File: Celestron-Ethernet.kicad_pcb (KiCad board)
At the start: 4 copper layers, 88.9 x 31.8 mm, 61 parts, among them J1 FTDI, J2 RJ45_Amphenol_RJMG1BD3B8K1ANR, J3 6P6C, SW1 SW_Push, SW2 SW_DIP_x02, U1 W5500, U2 ATmega328P-AU, U3 74AHC1G125, U4 NCV33375ST-3.3, Y1 8MHz, Y2 25MHz

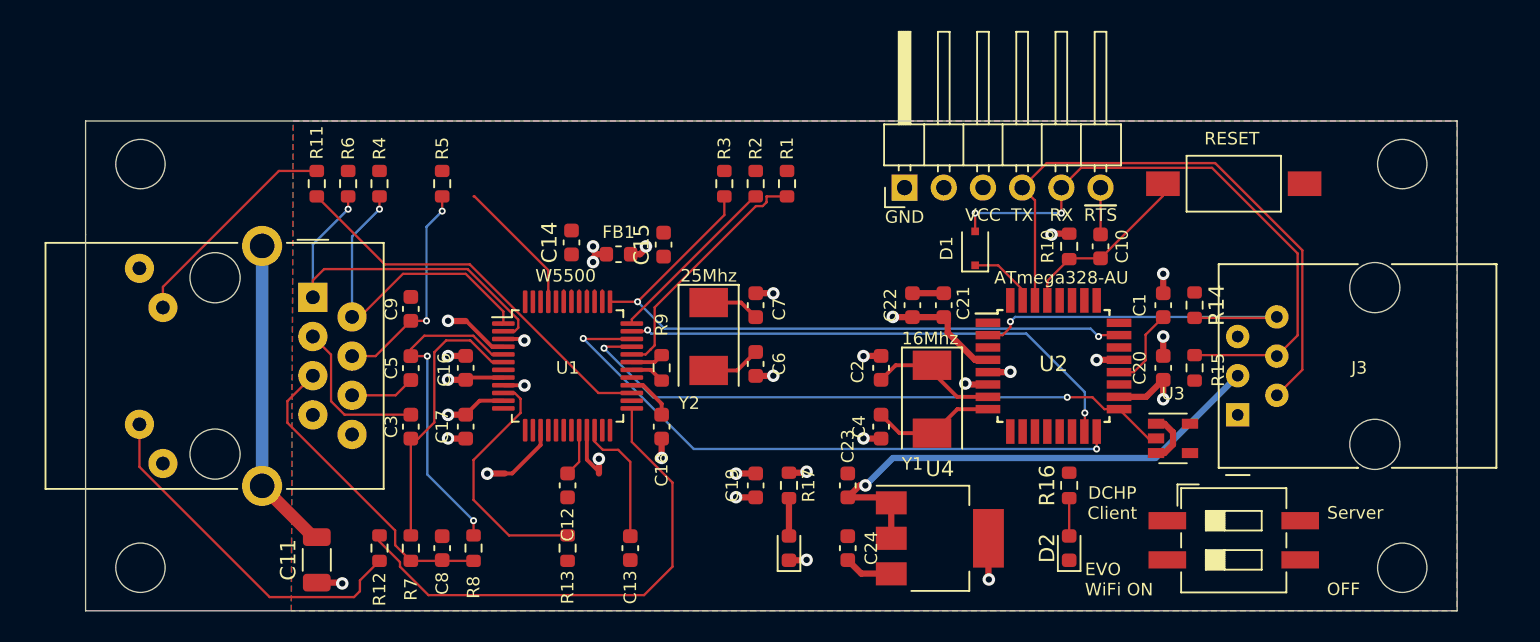
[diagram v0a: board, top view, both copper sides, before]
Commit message: Added GPS connectors
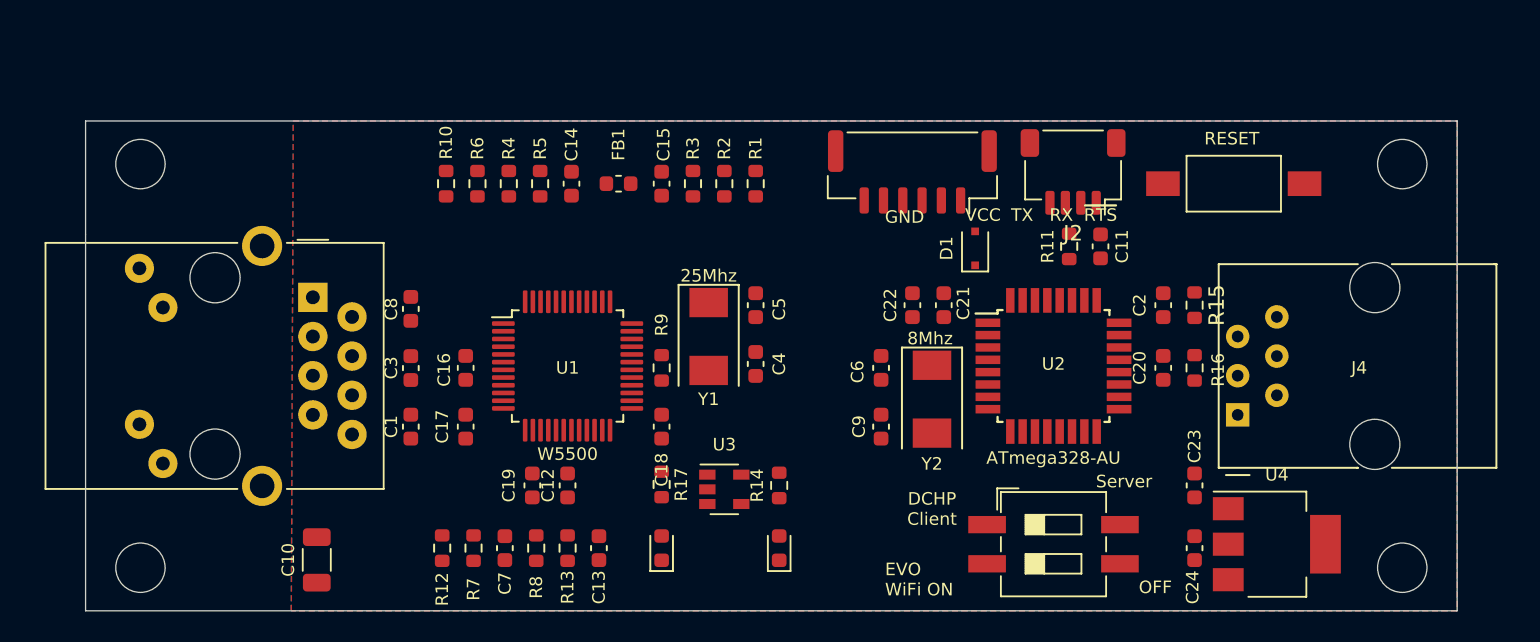
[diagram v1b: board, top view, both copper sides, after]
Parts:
- removed the C11 at (116.6, 111.0)
- removed the C6 at (145.0, 98.3)
- removed the C9 at (122.7, 94.7)
- removed the R11 at (116.6, 86.6)
- removed the R16 at (165.4, 106.2)
- removed the Y2 at (142.0, 96.5)
- added C1: 6.8nF, Capacitor_SMD:C_0603_1608Metric, F.Cu at (122.7, 102.4)
- added C10: 1nF/2KV, Capacitor_SMD:C_1206_3216Metric, F.Cu at (116.6, 111.0)
- added C4: 18pF, Capacitor_SMD:C_0603_1608Metric, F.Cu at (145.0, 98.3)
- added J3: RJ45_Amphenol_RJMG1BD3B8K1ANR, Connector_RJ:RJ45_Amphenol_RJMG1BD3B8K1ANR, F.Cu at (116.3, 94.0)
- added R10: 330R, Resistor_SMD:R_0603_1608Metric, F.Cu at (125.0, 86.6)
- added R14: 330R, Resistor_SMD:R_0603_1608Metric, F.Cu at (146.6, 106.2)
- added Y1: 25MHz, Crystal:Crystal_SMD_0603-2Pin_6.0x3.5mm, F.Cu at (142.0, 96.5)
- C5: value 6.8nF -> 18pF
- C7: value 18pF -> 10nF
- C8: value 10nF -> 22nF
- J1: footprint Connector_PinHeader_2.54mm:PinHeader_1x06_P2.54mm_Horizontal -> Connector_JST:JST_GH_SM06B-GHS-TB_1x06-1MP_P1.25mm_Horizontal
- J2: value RJ45_Amphenol_RJMG1BD3B8K1ANR -> Conn_01x04; footprint Connector_RJ:RJ45_Amphenol_RJMG1BD3B8K1ANR -> Connector_JST:JST_SH_SM04B-SRSS-TB_1x04-1MP_P1.00mm_Horizontal
- moved J2 49.9 mm to (165.6, 85.9), turned to 180 degrees
- moved U3 29.3 mm to (143.0, 106.4)
- moved C5 22.7 mm to (145.0, 94.5), turned to 270 degrees
- moved C7 22.6 mm to (128.8, 110.2)
- moved C23 22.5 mm to (173.5, 106.2)
- moved C24 22.5 mm to (173.5, 110.2)
- moved U4 21.8 mm to (178.8, 110.0)
- moved D2 18.8 mm to (146.6, 110.2)
- moved C8 15.6 mm to (122.7, 94.7)
- moved C19 14.5 mm to (130.6, 106.2)
- moved SW1 11.7 mm to (164.3, 110.0)
- moved R4 8.38 mm to (129.0, 86.6)
- moved R6 8.38 mm to (127.0, 86.6)
- moved R17 8.26 mm to (138.9, 106.1)
- moved D3 8.26 mm to (138.9, 110.2)
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- renumbered C10 to C11, C1 to C2, C2 to C6, C4 to C9, J3 to J4, R10 to R11, R14 to R15, R15 to R16, SW2 to SW1, SW1 to SW2, Y1 to Y2
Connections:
- net /D8 renamed /BUSY
- C3 pad 1: /RX+ -> /RD-
- C3 pad 2: /RD+ -> /RX-
- C5 pad 1: /RD- -> GND
- C5 pad 2: /RX- -> Net-(C5-Pad2)
- C7 pad 2: Net-(C7-Pad2) -> /RCT
- C8 pad 2: /RCT -> /TCT
- J1 pad 1: GND -> (no net)
- J1 pad 3: VCC -> /GTX
- J1 pad 4: /RXI -> /GRX
- J1 pad 5: /TXO -> VCC
- J1 pad 6: /DTR -> (no net)
- J4 pad 1: Net-(J3-Pad1) -> /DTR
- R9 pad 1: Net-(C7-Pad2) -> Net-(C5-Pad2)
- U1 pad 12: Net-(U1-Pad12) -> (no net)
- U1 pad 13: Net-(U1-Pad13) -> (no net)
- U1 pad 18: Net-(U1-Pad18) -> (no net)
- U1 pad 24: Net-(U1-Pad24) -> (no net)
- U1 pad 26: Net-(U1-Pad26) -> (no net)
- U1 pad 31: Net-(C7-Pad2) -> Net-(C5-Pad2)
- U1 pad 46: Net-(U1-Pad46) -> (no net)
- U1 pad 47: Net-(U1-Pad47) -> (no net)
- U1 pad 7: Net-(U1-Pad7) -> (no net)
- U2 pad 1: Net-(U2-Pad1) -> (no net)
- U2 pad 10: Net-(U2-Pad10) -> /GRX
- U2 pad 11: Net-(U2-Pad11) -> /GTX
- U2 pad 13: Net-(U2-Pad13) -> (no net)
- U2 pad 14: Net-(U2-Pad14) -> (no net)
- U2 pad 19: Net-(U2-Pad19) -> (no net)
- U2 pad 22: Net-(U2-Pad22) -> (no net)
- U2 pad 24: Net-(U2-Pad24) -> (no net)
- U2 pad 25: Net-(U2-Pad25) -> (no net)
- U2 pad 26: Net-(U2-Pad26) -> (no net)
- U2 pad 27: Net-(U2-Pad27) -> (no net)
- U2 pad 28: Net-(U2-Pad28) -> (no net)
- U2 pad 32: Net-(U2-Pad32) -> (no net)
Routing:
- net /~RST: track 43.1 -> 0.00 mm, vias 2 -> 0
- net /MISO: track 40.5 -> 0.00 mm, vias 2 -> 0
- net /SCK: track 40.0 -> 0.00 mm, vias 2 -> 0
- net /TXO: track 39.2 -> 0.00 mm, vias 2 -> 0
- net /RXI: track 38.9 -> 0.00 mm
- net VCC: track 34.8 -> 0.00 mm, vias 7 -> 0
- net +12V: track 34.1 -> 0.00 mm, vias 1 -> 0
- net /MOSI: track 33.6 -> 0.00 mm, vias 2 -> 0
- net /LINKLED: track 33.1 -> 0.00 mm
- net GND: track 32.3 -> 0.00 mm, vias 17 -> 0
- net /ACTLED: track 25.7 -> 0.00 mm
- net /TD+: track 25.2 -> 0.00 mm, vias 1 -> 0
- net /BUSY: track 24.8 -> 0.00 mm, vias 1 -> 0
- net /LEDY_K: track 23.2 -> 0.00 mm
- net +3.3VA: track 23.0 -> 0.00 mm, vias 7 -> 0
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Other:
- board text added: "8Mhz"
- board text removed: "16Mhz"

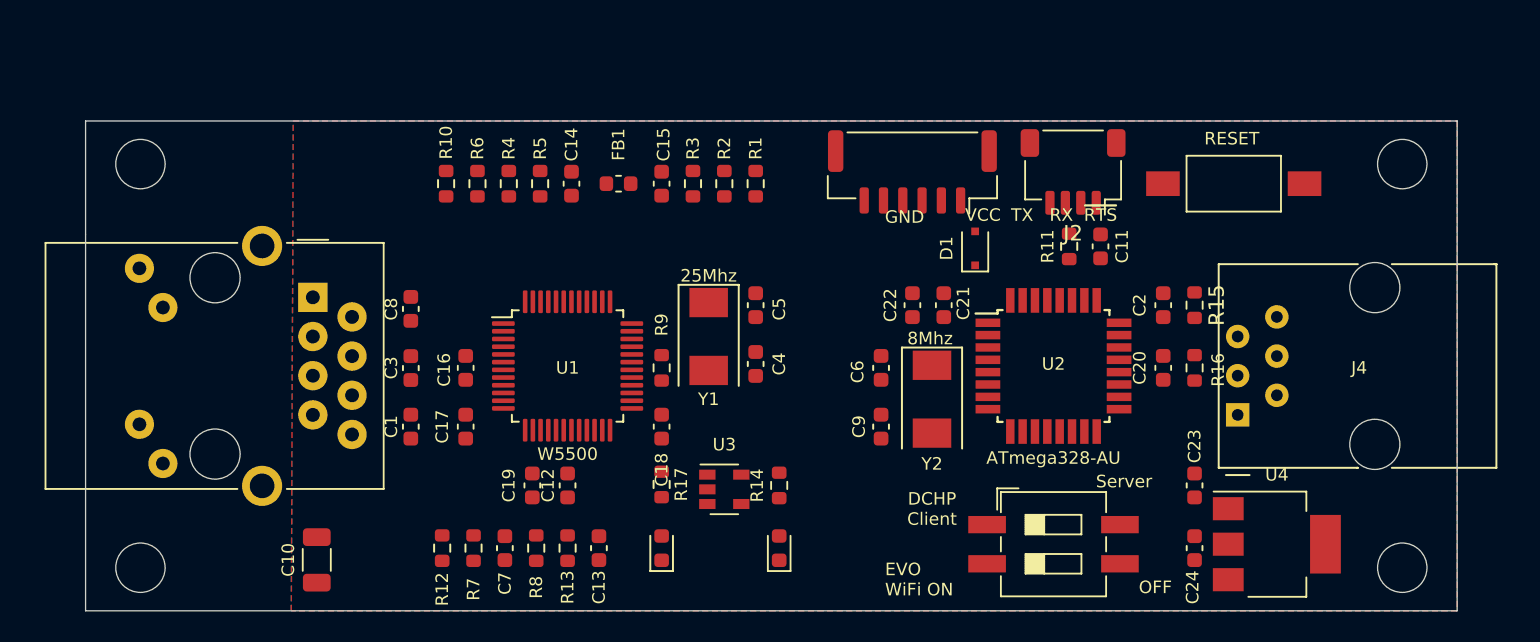
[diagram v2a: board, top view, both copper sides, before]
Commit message: W5500 fixes
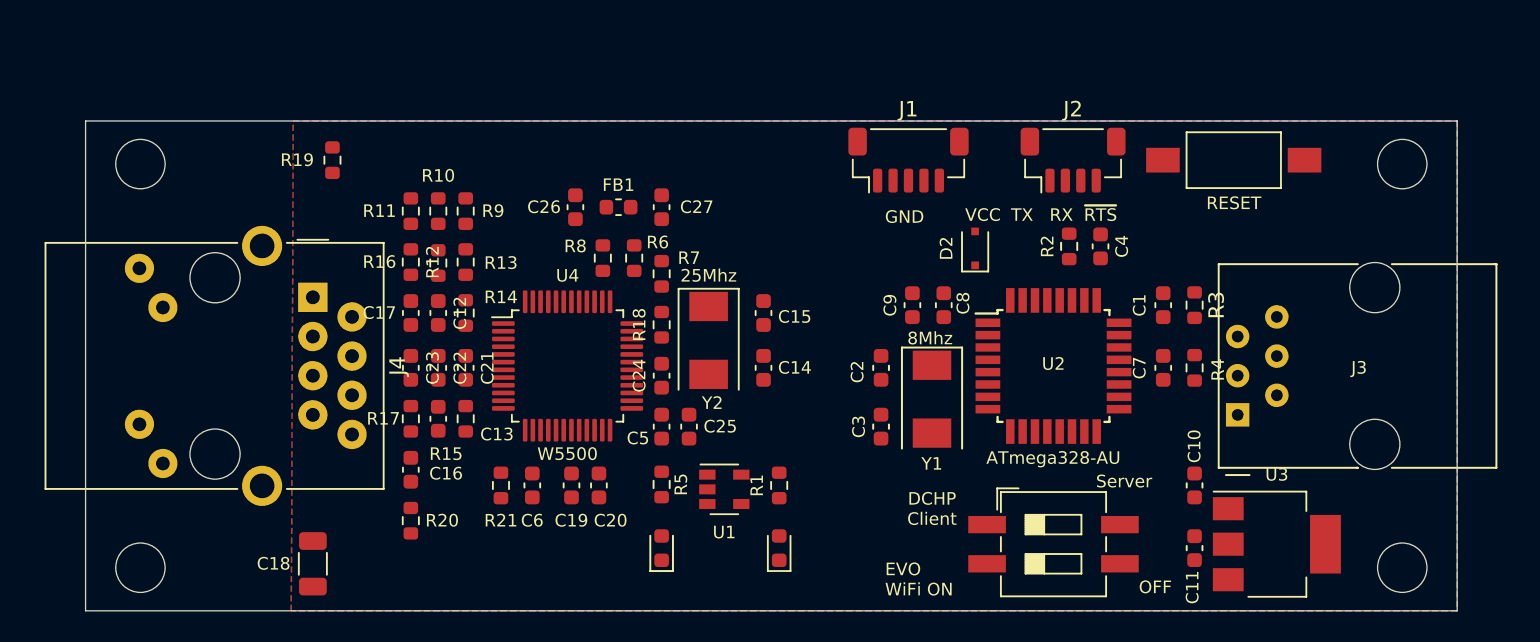
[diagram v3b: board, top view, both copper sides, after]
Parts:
- removed the C1 at (122.7, 102.4)
- removed the C10 at (116.6, 111.0)
- removed the C3 at (122.7, 98.6)
- removed the C4 at (145.0, 98.3)
- removed the C5 at (145.0, 94.5)
- removed the C7 at (128.8, 110.2)
- removed the C8 at (122.7, 94.7)
- removed the J3 at (116.3, 94.0)
- removed the R1 at (145.0, 86.6)
- removed the R2 at (143.0, 86.6)
- removed the R3 at (141.0, 86.6)
- removed the R4 at (129.0, 86.6)
- removed the R5 at (131.1, 86.6)
- removed the U1 at (132.8, 98.4)
- removed the Y1 at (142.0, 96.5)
- added C18: 1nF/2KV, Capacitor_SMD:C_1206_3216Metric, F.Cu at (116.3, 111.3)
- added C19: 4.7uF, Capacitor_SMD:C_0603_1608Metric, F.Cu at (133.1, 106.2)
- added C20: 10nF, Capacitor_SMD:C_0603_1608Metric, F.Cu at (134.9, 106.2)
- added C21: 100nF, Capacitor_SMD:C_0603_1608Metric, F.Cu at (126.2, 98.6)
- added C22: 1uF, Capacitor_SMD:C_0603_1608Metric, F.Cu at (124.5, 98.6)
- added C23: 10uF, Capacitor_SMD:C_0603_1608Metric, F.Cu at (122.7, 98.6)
- added C24: 100nF, Capacitor_SMD:C_0603_1608Metric, F.Cu at (138.9, 99.1)
- added C25: 10uF, Capacitor_SMD:C_0603_1608Metric, F.Cu at (140.7, 102.4)
- added C26: 100nF, Capacitor_SMD:C_0603_1608Metric, F.Cu at (133.3, 88.1)
- added C27: 100nF, Capacitor_SMD:C_0603_1608Metric, F.Cu at (138.9, 88.1)
- added J4: RJ45_Amphenol_RJMG1BD3B8K1ANR, Connector_RJ:RJ45_Amphenol_RJMG1BD3B8K1ANR, F.Cu at (116.3, 94.0)
- added R11: 49R9, Resistor_SMD:R_0603_1608Metric, F.Cu at (122.7, 88.4)
- added R14: 3R3, Resistor_SMD:R_0603_1608Metric, F.Cu at (126.2, 95.0)
- added R15: 3R3, Resistor_SMD:R_0603_1608Metric, F.Cu at (126.2, 101.9)
- added R16: 49R9, Resistor_SMD:R_0603_1608Metric, F.Cu at (126.2, 91.7)
- added R17: 49R9, Resistor_SMD:R_0603_1608Metric, F.Cu at (122.7, 101.9)
- added R18: 1M, Resistor_SMD:R_0603_1608Metric, F.Cu at (138.9, 95.8)
- added R19: 330R, Resistor_SMD:R_0603_1608Metric, F.Cu at (117.6, 85.1)
- added R20: 330R, Resistor_SMD:R_0603_1608Metric, F.Cu at (122.7, 108.5)
- added R21: 12.4K, Resistor_SMD:R_0603_1608Metric, F.Cu at (128.5, 106.2)
- added U4: W5500, Package_QFP:LQFP-48_7x7mm_P0.5mm, F.Cu at (132.8, 98.4)
- added Y2: 25MHz, Crystal:Crystal_SMD_0603-2Pin_6.0x3.5mm, F.Cu at (142.0, 96.8)
- C12: value 4.7uF -> 6.8nF
- C13: value 10nF -> 6.8nF
- C14, C15: value 100nF -> 18pF
- C16: value 100nF -> 10nF
- C17: value 10uF -> 22nF
- J1: value FTDI -> Joystick; footprint Connector_JST:JST_GH_SM06B-GHS-TB_1x06-1MP_P1.25mm_Horizontal -> Connector_JST:JST_SH_BM05B-SRSS-TB_1x05-1MP_P1.00mm_Vertical
- J2: value Conn_01x04 -> GPS; footprint Connector_JST:JST_SH_SM04B-SRSS-TB_1x04-1MP_P1.00mm_Horizontal -> Connector_JST:JST_SH_BM04B-SRSS-TB_1x04-1MP_P1.00mm_Vertical
- R10: value 330R -> 10R
- R12: value 330R -> 3R3
- R13: value 12.4K -> 3R3
- R6: value 49R9 -> 10K
- R7, R8: value 82R -> 10K
- R9: value 1M -> 49R9
- moved R7 21.6 mm to (138.9, 92.5)
- moved R13 20.3 mm to (124.5, 91.8), turned to 270 degrees
- moved R8 19.3 mm to (135.1, 91.4)
- moved R12 18.7 mm to (122.7, 91.7), turned to 270 degrees
- moved C14 17.2 mm to (145.5, 98.6), turned to 270 degrees
- moved R9 16.3 mm to (126.2, 88.4), turned to 90 degrees
- moved C12 14.0 mm to (124.5, 95.0), turned to 270 degrees
- moved C13 13.4 mm to (124.5, 101.9), turned to 270 degrees
- moved R6 11.2 mm to (137.2, 91.4), turned to 270 degrees
- moved C15 10.7 mm to (145.5, 95.0)
- moved C17 8.18 mm to (122.7, 95.0)
- moved C16 7.50 mm to (122.7, 105.2)
- moved R10 1.85 mm to (124.5, 88.4), turned to 90 degrees
- moved FB1 1.52 mm to (136.1, 88.1)
- moved SW2 1.52 mm to (176.0, 85.1)
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- renumbered C2 to C1, C23 to C10, C24 to C11, C6 to C2, C9 to C3, C11 to C4, C18 to C5, C19 to C6, C20 to C7, C21 to C8, C22 to C9, D2 to D1, D1 to D2, J4 to J3, R14 to R1, R11 to R2, R15 to R3, R16 to R4, R17 to R5, U3 to U1, U4 to U3, Y2 to Y1
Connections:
- C12 pad 1: GND -> /W5500/RX+
- C12 pad 2: Net-(C12-Pad2) -> /W5500/RD+
- C13 pad 1: GND -> /W5500/RD-
- C13 pad 2: Net-(C13-Pad2) -> /W5500/RX-
- C14 pad 1: +3.3VA -> GND
- C14 pad 2: GND -> Net-(C14-Pad2)
- C15 pad 1: VCC -> GND
- C15 pad 2: GND -> Net-(C15-Pad2)
- C16 pad 1: +3.3VA -> GND
- C16 pad 2: GND -> /W5500/RCT
- C17 pad 1: +3.3VA -> GND
- C17 pad 2: GND -> /W5500/TCT
- J1 pad 1: (no net) -> GND
- J1 pad 2: GND -> /IRQ
- J1 pad 3: /GTX -> /SDA
- J1 pad 4: /GRX -> /SCL
- R10 pad 1: /LEDG_K -> /W5500/TCT
- R10 pad 2: /ACTLED -> +3.3VA
- R12 pad 1: /LEDY_K -> /W5500/TD+
- R12 pad 2: /LINKLED -> /W5500/TXP
- R13 pad 1: GND -> /W5500/TD-
- R13 pad 2: Net-(R13-Pad2) -> /W5500/TXN
- R6 pad 1: /TD+ -> VCC
- R6 pad 2: +3.3VA -> Net-(R6-Pad2)
- R7 pad 1: /RX+ -> VCC
- R7 pad 2: /RCT -> Net-(R7-Pad2)
- R8 pad 1: /RX- -> VCC
- R8 pad 2: /RCT -> /~RST
- R9 pad 1: Net-(C5-Pad2) -> /W5500/TD-
- R9 pad 2: Net-(C4-Pad2) -> +3.3VA
- U2 pad 26: (no net) -> /IRQ
- U2 pad 27: (no net) -> /SDA
- U2 pad 28: (no net) -> /SCL

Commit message: cleanup
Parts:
- moved R19 14.2 mm to (131.6, 87.9)
- moved R7 7.03 mm to (145.8, 90.9)
- moved R6 6.12 mm to (143.3, 90.9)
- moved R8 5.61 mm to (140.7, 90.9)
- moved C27 4.50 mm to (143.3, 86.9)
- moved C25 4.13 mm to (144.8, 103.1)
- moved Y2 4.07 mm to (146.1, 96.9)
- moved C15 4.07 mm to (149.6, 95.1)
- moved C14 4.07 mm to (149.6, 98.7)
- moved U1 3.81 mm to (146.1, 108.7)
- moved R15 3.42 mm to (128.8, 104.1)
- moved C5 3.39 mm to (142.2, 103.1)
- moved R18 3.39 mm to (142.2, 95.0)
- moved R20 3.31 mm to (126.0, 108.2)
- moved C24 3.30 mm to (142.2, 99.2)
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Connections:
- J1 pad 2: /IRQ -> /SCL
- J1 pad 4: /SCL -> /IRQ
- J4 pad R7: (no net) -> Net-(J4-PadR7)
- U2 pad 1: (no net) -> Net-(U2-Pad1)
- U2 pad 13: (no net) -> Net-(U2-Pad13)
- U2 pad 14: (no net) -> Net-(U2-Pad14)
- U2 pad 19: (no net) -> Net-(U2-Pad19)
- U2 pad 22: (no net) -> Net-(U2-Pad22)
- U2 pad 24: (no net) -> Net-(U2-Pad24)
- U2 pad 25: (no net) -> Net-(U2-Pad25)
- U2 pad 32: (no net) -> Net-(U2-Pad32)
- U4 pad 12: (no net) -> Net-(U4-Pad12)
- U4 pad 13: (no net) -> Net-(U4-Pad13)
- U4 pad 18: (no net) -> Net-(U4-Pad18)
- U4 pad 24: (no net) -> Net-(U4-Pad24)
- U4 pad 26: (no net) -> Net-(U4-Pad26)
- U4 pad 46: (no net) -> Net-(U4-Pad46)
- U4 pad 47: (no net) -> Net-(U4-Pad47)
- U4 pad 7: (no net) -> Net-(U4-Pad7)
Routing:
- removed copper zone on In1.Cu, net GNDPWR

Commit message: cleanup
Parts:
- moved R2 5.85 mm to (171.2, 90.4), turned to 90 degrees
- moved C26 3.82 mm to (134.2, 84.3)
- moved D2 3.32 mm to (162.6, 90.4)
- moved R7 2.69 mm to (146.7, 88.4)
- moved R6 2.62 mm to (143.9, 88.4)
- moved C27 2.62 mm to (143.9, 84.3)
- moved R8 2.57 mm to (141.1, 88.4)
- moved FB1 2.54 mm to (139.2, 84.3)
- moved R18 2.25 mm to (143.9, 96.5)
- moved C24 2.16 mm to (143.9, 100.6)
- moved C14 2.10 mm to (150.5, 100.6)
- moved Y2 2.01 mm to (147.2, 98.6)
- moved C5 1.91 mm to (141.1, 104.6)
- moved C25 1.76 mm to (143.9, 104.6)
- moved R5 1.76 mm to (141.1, 108.7)
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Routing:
- net /W5500/RXP: track 0.00 -> 3.73 mm
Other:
- board text added: "GPS"
- board text added: "Keypad"
- board text removed: "GND"
- board text removed: "RX"
- board text removed: "TX"
- board text removed: "VCC"
- board text removed: "~RTS"

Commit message: cleanup
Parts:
- moved R5 29.9 mm to (170.9, 106.7)
- moved D3 29.9 mm to (170.9, 110.7)
- moved R16 12.6 mm to (126.1, 104.8), turned to 270 degrees
- moved C12 8.68 mm to (123.3, 104.8)
- moved C17 8.38 mm to (123.3, 88.1)
- moved R14 8.26 mm to (128.8, 104.8), turned to 90 degrees
- moved R9 6.73 mm to (123.3, 92.3)
- moved R12 5.59 mm to (128.8, 92.3)
- moved R13 5.14 mm to (128.8, 88.1)
- moved R11 4.90 mm to (126.1, 92.3)
- moved R1 4.16 mm to (150.5, 104.6)
- moved C22 4.07 mm to (126.1, 96.5)
- moved C23 4.07 mm to (123.3, 96.5)
- moved C21 4.06 mm to (128.8, 96.5)
- moved C13 3.94 mm to (126.1, 100.7)
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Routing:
- net /W5500/RXP: track 3.73 -> 0.00 mm
